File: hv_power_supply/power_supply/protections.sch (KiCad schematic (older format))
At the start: 15 parts, among them J2 CONN_01x02, K2 LI12-1A85(NO), Q2 SSM3K333R, Q3 SSM3K333R, Q4 FQD2N60CTM, U6 CPC1117NTR

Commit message: Update output relay
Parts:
- removed D4: D_Zener_18V, footprints:DO-214AA, symbol formula:D_Zener_18V
- removed D5: Diode_600V_1A_SM, footprints:Diode_600V_1A_SM, symbol formula:Diode_600V_1A_SM
- removed K2: LI12-1A85(NO), footprints:Meder-LI12, symbol formula:LI12-1A85(NO)
- removed Q2: SSM3K333R, footprints:SOT-23F, symbol formula:SSM3K333R
- added F1: F_1A_600V, footprints:Fuse_1A_600V, symbol formula:F_1A_600V
- added K1: CPC1979J, footprints:TO381P2016X515X2916-4, symbol formula:CPC1979J
- added Q4: SSM3K333R, footprints:SOT-23F, symbol formula:SSM3K333R
- renumbered D1 to D4, Q3 to Q2, Q4 to Q3, R1 to R23
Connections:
- wire segments 24 -> 19
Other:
- note added: "Normally Closed SSR"
- note added: "Normally Open SSR"
- note removed: "Normally Closed"
- note removed: "To outside switch"

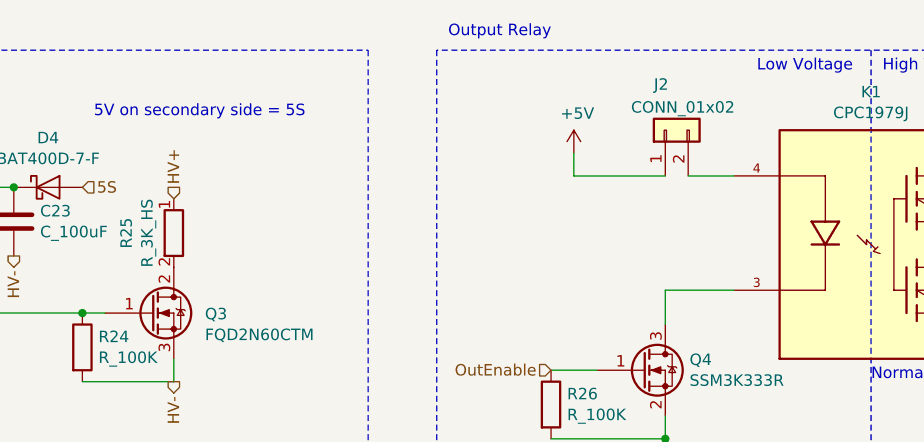
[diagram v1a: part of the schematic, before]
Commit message: Add resistor to output relay
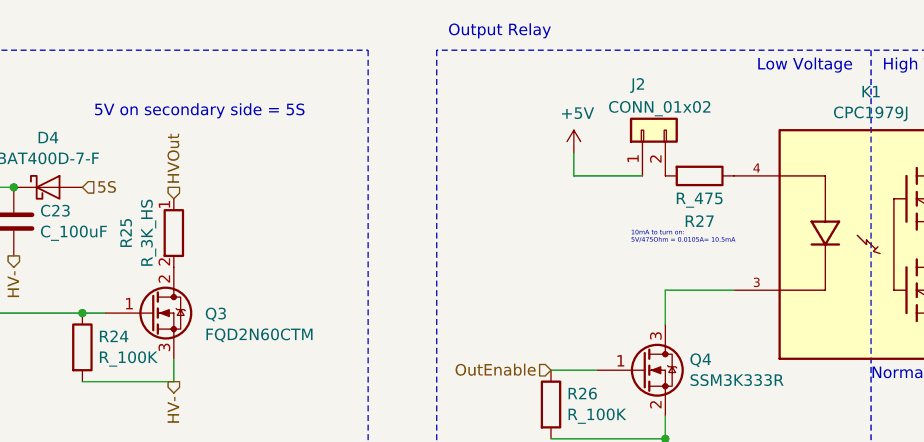
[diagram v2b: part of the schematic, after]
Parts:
- added R27: R_475, footprints:R_0805_OEM, symbol formula:R_475
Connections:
- net HV+: no longer R25.1
- net HVOut: now also R25.1
- net at K1.4: now also R27.1; no longer J2.2 (Pin_2)
- new net: J2.2 (Pin_2), R27.2
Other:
- note added: "10mA to turn on:\n5V/475Ohm = 0.0105A= 10.5mA"
- moved on the sheet: J2
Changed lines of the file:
@@
 $Descr A4 11693 8268
 encoding utf-8
-Sheet 1 1
+Sheet 5 5
 Title ""
 Date ""
@@
 HV-
 Text HLabel 4000 1450 1    50   Input ~ 0
-HV+
+HVOut
 $Comp
 L formula:R_3K_HS R25
@@
 L formula:CONN_01x02 J2
 U 1 1 6035D5F6
-P 6150 1150
-F 0 "J2" V 6350 1200 50  0000 R CNN
-F 1 "CONN_01x02" V 6250 1300 50  0000 R CNN
-F 2 "Connector_PinHeader_2.54mm:PinHeader_1x02_P2.54mm_Vertical" H 6050 1150 50  0001 C CNN
-F 3 "https://katalog.we-online.de/em/datasheet/6130xx11121.pdf" H 6150 1250 50  0001 C CNN
-F 4 "DK" H 6250 1350 50  0001 C CNN "MFN"
-F 5 "732-5315-ND" H 6350 1450 50  0001 C CNN "MPN"
-	1    6150 1150
+P 6050 1150
+F 0 "J2" V 6250 1200 50  0000 R CNN
+F 1 "CONN_01x02" V 6150 1300 50  0000 R CNN
+F 2 "Connector_PinHeader_2.54mm:PinHeader_1x02_P2.54mm_Vertical" H 5950 1150 50  0001 C CNN
+F 3 "https://katalog.we-online.de/em/datasheet/6130xx11121.pdf" H 6050 1250 50  0001 C CNN
+F 4 "DK" H 6150 1350 50  0001 C CNN "MFN"
+F 5 "732-5315-ND" H 6250 1450 50  0001 C CNN "MPN"
+	1    6050 1150
 	0    -1   -1   0
 $EndComp
-Wire Wire Line
-	6450 1350 6250 1350
-Wire Wire Line
-	6150 1350 5750 1350
 Wire Wire Line
 	5750 1350 5750 1250
@@
 Text Notes 7100 900  0    50   ~ 0
 High Voltage
+Text Notes 6000 1650 0    20   ~ 0
+10mA to turn on:\n5V/475Ohm = 0.0105A= 10.5mA
+$Comp
+L formula:R_475 R27
+U 1 1 6039FDDB
+P 6300 1350
+F 0 "R27" V 6500 1350 50  0000 C CNN
+F 1 "R_475" V 6400 1350 50  0000 C CNN
+F 2 "footprints:R_0805_OEM" H 6230 1350 50  0001 C CNN
+F 3 "http://www.yageo.com.tw/exep/pages/download/literatures/PYu-R_INT-thick_7.pdf" H 6380 1350 50  0001 C CNN
+F 4 "DK" H 6300 1350 60  0001 C CNN "MFN"
+F 5 "311-475CRCT-ND" H 6300 1350 60  0001 C CNN "MPN"
+F 6 "https://www.digikey.com/products/en?keywords=311-475CRCT-ND" H 6780 1750 60  0001 C CNN "PurchasingLink"
+	1    6300 1350
+	0    1    1    0
+$EndComp
+Wire Wire Line
+	6050 1350 5750 1350
 $EndSCHEMATC

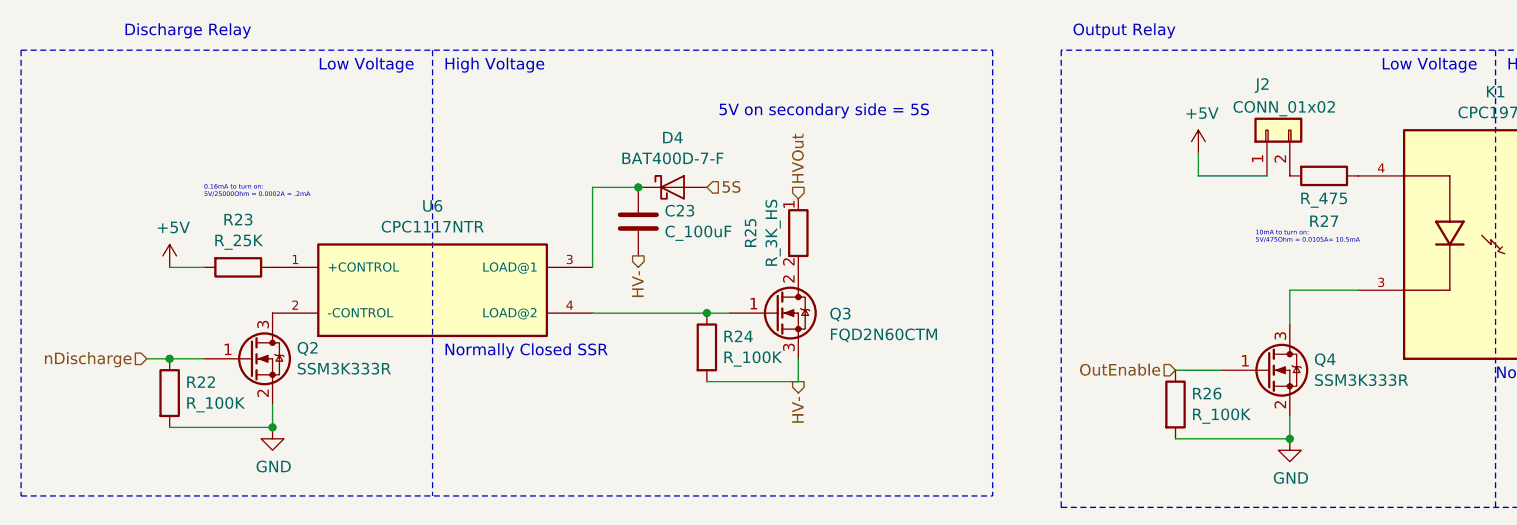
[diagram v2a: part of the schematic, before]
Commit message: Tie inputs to relays together
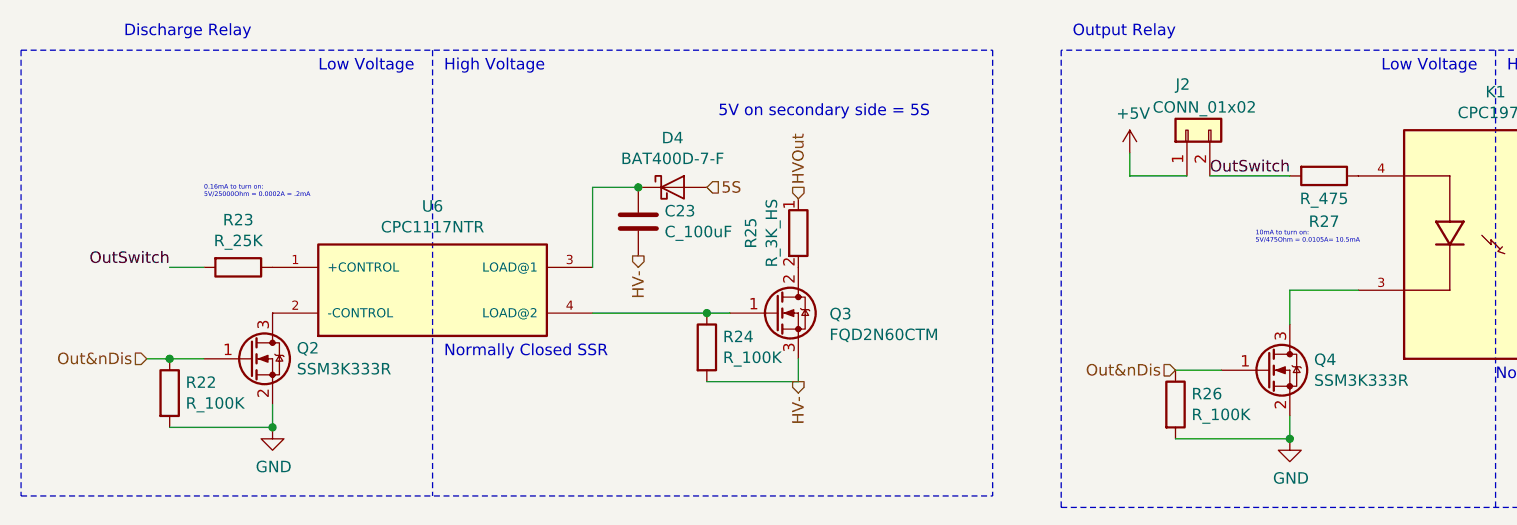
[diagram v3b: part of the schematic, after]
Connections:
- net nDischarge is gone; now on net Out&nDis: Q2.1 (G), R22.1
- net +5V: no longer R23.2
- net OutSwitch: now reaches J2.2 (Pin_2), R27.2
- net OutSwitch: now also R23.2
- net OutEnable renamed Out&nDis
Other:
- moved on the sheet: J2
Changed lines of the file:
@@
 	1250 2450 1700 2450
 Text HLabel 1150 2150 0    50   Input ~ 0
-nDischarge
+Out&nDis
 Wire Wire Line
 	1250 2150 1150 2150
@@
 Connection ~ 3300 1400
 $Comp
-L power:+5V #PWR071
-U 1 1 6029A8EE
-P 1250 1750
-F 0 "#PWR071" H 1250 1600 50  0001 C CNN
-F 1 "+5V" H 1265 1923 50  0000 C CNN
-F 2 "" H 1250 1750 50  0001 C CNN
-F 3 "" H 1250 1750 50  0001 C CNN
-	1    1250 1750
-	1    0    0    -1
-$EndComp
-$Comp
 L formula:R_25K R23
 U 1 1 602A28CD
@@
 L formula:CONN_01x02 J2
 U 1 1 6035D5F6
-P 6050 1150
-F 0 "J2" V 6250 1200 50  0000 R CNN
-F 1 "CONN_01x02" V 6150 1300 50  0000 R CNN
-F 2 "Connector_PinHeader_2.54mm:PinHeader_1x02_P2.54mm_Vertical" H 5950 1150 50  0001 C CNN
-F 3 "https://katalog.we-online.de/em/datasheet/6130xx11121.pdf" H 6050 1250 50  0001 C CNN
-F 4 "DK" H 6150 1350 50  0001 C CNN "MFN"
-F 5 "732-5315-ND" H 6250 1450 50  0001 C CNN "MPN"
-	1    6050 1150
+P 5700 1150
+F 0 "J2" V 5900 1200 50  0000 R CNN
+F 1 "CONN_01x02" V 5800 1300 50  0000 R CNN
+F 2 "Connector_PinHeader_2.54mm:PinHeader_1x02_P2.54mm_Vertical" H 5600 1150 50  0001 C CNN
+F 3 "https://katalog.we-online.de/em/datasheet/6130xx11121.pdf" H 5700 1250 50  0001 C CNN
+F 4 "DK" H 5800 1350 50  0001 C CNN "MFN"
+F 5 "732-5315-ND" H 5900 1450 50  0001 C CNN "MPN"
+	1    5700 1150
 	0    -1   -1   0
 $EndComp
 Wire Wire Line
-	5750 1350 5750 1250
+	5450 1350 5450 1250
 $Comp
 L power:+5V #PWR073
 U 1 1 60366556
-P 5750 1250
-F 0 "#PWR073" H 5750 1100 50  0001 C CNN
-F 1 "+5V" H 5765 1423 50  0000 C CNN
-F 2 "" H 5750 1250 50  0001 C CNN
-F 3 "" H 5750 1250 50  0001 C CNN
-	1    5750 1250
+P 5450 1250
+F 0 "#PWR073" H 5450 1100 50  0001 C CNN
+F 1 "+5V" H 5465 1423 50  0000 C CNN
+F 2 "" H 5450 1250 50  0001 C CNN
+F 3 "" H 5450 1250 50  0001 C CNN
+	1    5450 1250
 	1    0    0    -1
 $EndComp
 Text HLabel 5650 2200 0    50   Input ~ 0
-OutEnable
+Out&nDis
 $Comp
 L formula:R_100K R26
@@
 	0    1    1    0
 $EndComp
-Wire Wire Line
-	6050 1350 5750 1350
+Text Label 5800 1350 0    50   ~ 0
+OutSwitch
+Text Label 1250 1750 2    50   ~ 0
+OutSwitch
+Wire Wire Line
+	5700 1350 5450 1350
+Wire Wire Line
+	5800 1350 6150 1350
 $EndSCHEMATC

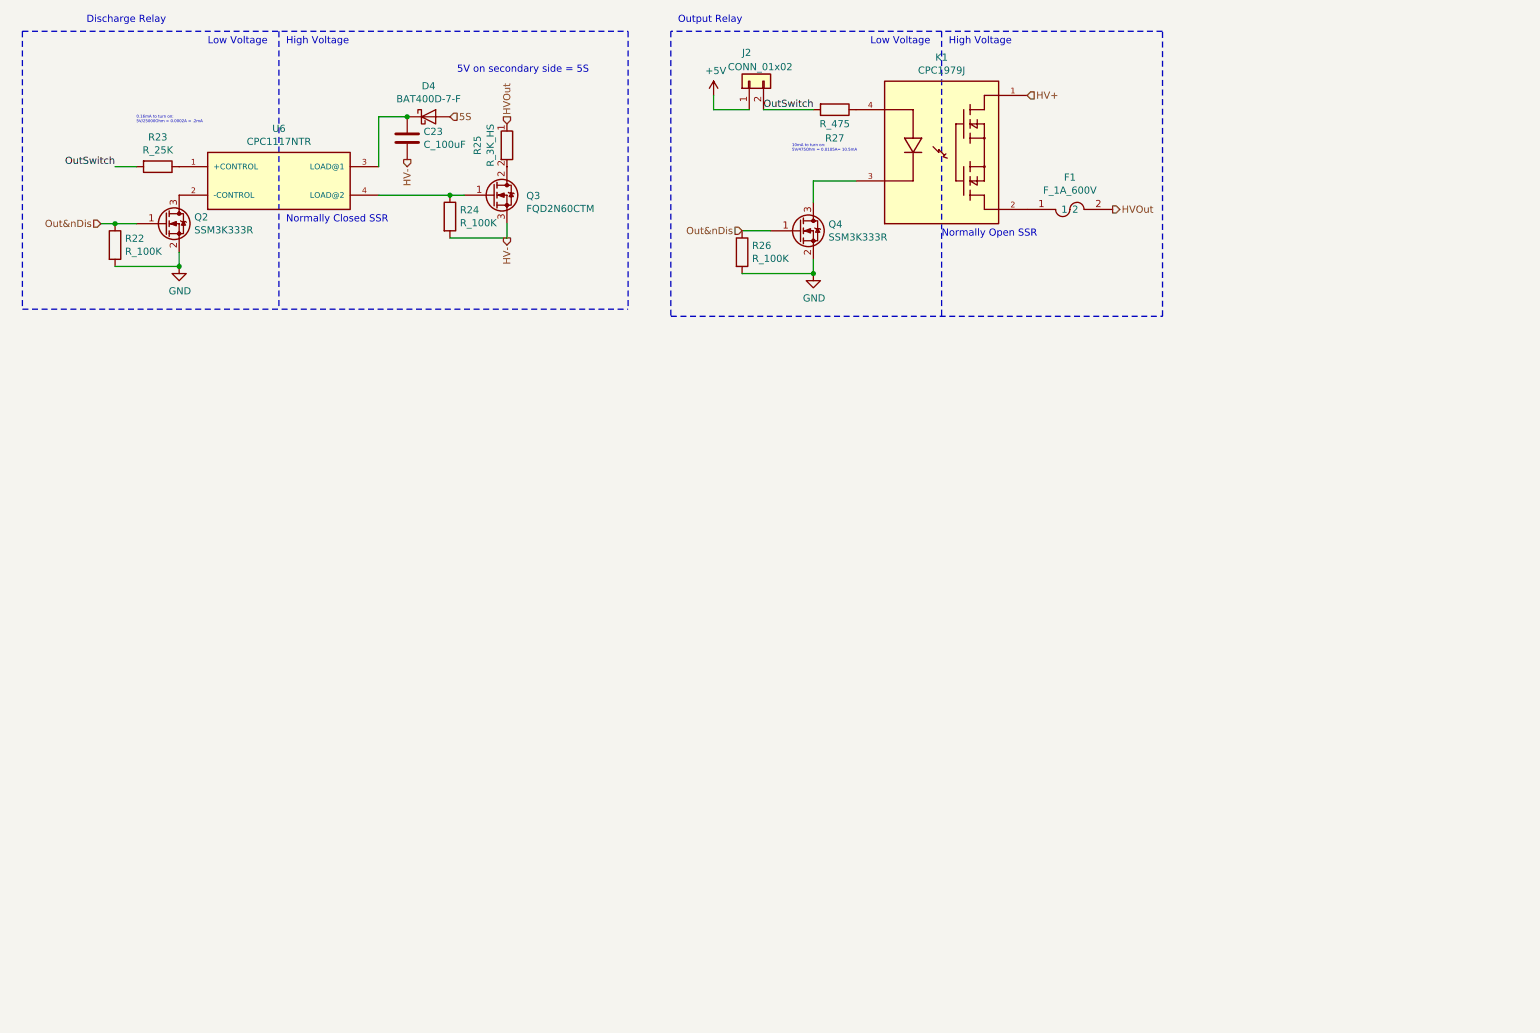
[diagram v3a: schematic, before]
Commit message: make schematic sheets talk to each other
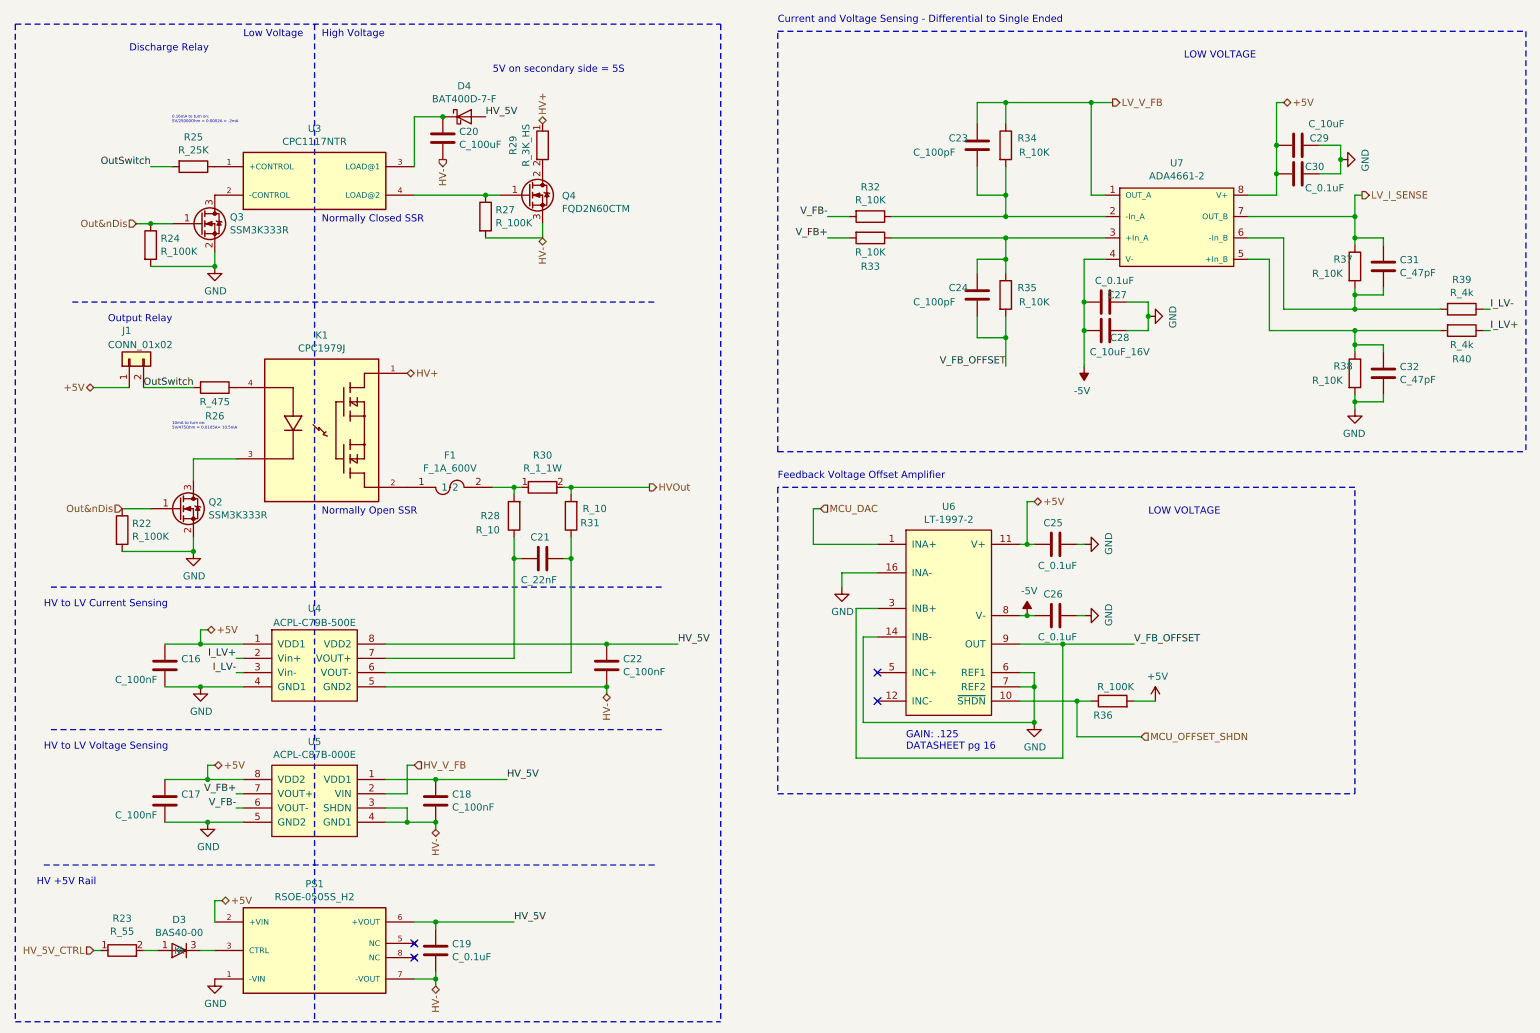
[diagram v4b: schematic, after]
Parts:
- added C16, C17, C18, C22: C_100nF, footprints:C_0603_1608Metric, symbol formula:C_100nF
- added C19, C25, C26, C27, C30: C_0.1uF, footprints:C_0805_OEM, symbol formula:C_0.1uF
- added C21: C_22nF, footprints:C_0805_OEM, symbol formula:C_22nF
- added C23, C24: C_100pF, footprints:C_0805_OEM, symbol formula:C_100pF
- added C28: C_10uF_16V, footprints:C_0805_OEM, symbol formula:C_10uF_16V
- added C29: C_10uF, footprints:C_0805_OEM, symbol formula:C_10uF_16V
- added C31, C32: C_47pF, footprints:C_0805_OEM, symbol formula:C_47pF
- added D3: BAS40-00, Package_TO_SOT_SMD:SOT-23, symbol formula:BAS40-00
- added PS1: RSOE-0505S_H2, footprints:H2, symbol formula:RSOE-0505S_H2
- added R23: R_55, symbol formula:R_55
- added R28, R31: R_10, footprints:R_0805_OEM, symbol formula:R_10
- added R30: R_1_1W, formula:R_2512_LARGE, symbol formula:R_1_1W
- added R32, R33, R34, R35, R37, R38: R_10K, footprints:R_0805_OEM, symbol formula:R_10K
- added R36: R_100K, footprints:R_0805_OEM, symbol formula:R_100K
- added R39, R40: R_4k, footprints:R_0805_OEM, symbol formula:R_4k
- added U4: ACPL-C79B-500E, footprints:SSO-8, symbol formula:ACPL-C79B-500E
- added U5: ACPL-C87B-000E, formula:SSO-8, symbol formula:ACPL-C87B-000E
- added U6: LT-1997-2, formula:16(12)-MSOP, symbol formula:LT-1997-2
- added U7: ADA4661-2, footprints:SOP65P490X110-8N, symbol formula:ADA4661-2
- renumbered C23 to C20, J2 to J1, Q4 to Q2, Q2 to Q3, Q3 to Q4, R26 to R22, R22 to R24, R23 to R25, R27 to R26, R24 to R27, R25 to R29, U6 to U3
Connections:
- net +5V: now also C16.1, C17.1, C25.1, C29.1, C30.2, PS1.2 (+VIN), R36.2, U4.1 (VDD1), U5.8 (VDD2), U6.11 (V+), U7.8 (V+)
- net GND: now also C16.2, C17.2, C25.2, C26.2, C27.2, C28.2, C29.2, C30.1, C32.2, PS1.1 (-VIN), R38.2, U4.4 (GND1), U5.5 (GND2), U6.14 (INB-), U6.16 (INA-), U6.6 (REF1), U6.7 (REF2)
- net HV+: now also R29.1
- net HV-: now also C18.2, C19.2, C22.2, PS1.7 (-VOUT), U4.5 (GND2), U5.3 (SHDN), U5.4 (GND1)
- net HVOut: now also R30.2, R31.2; no longer F1.2, R29.1
- net 5S renamed HV_5V
- net HV_5V: now also C18.1, C19.1, C22.1, PS1.6 (+VOUT), U4.8 (VDD2), U5.1 (VDD1)
- new net: F1.2, R28.2, R30.1
- new net: D3.3 (K), PS1.3 (CTRL)
- new net: C21.1, R28.1, U4.7 (VOUT+)
- new net: C21.2, R31.1, U4.6 (VOUT-)
- new net: C23.2, R32.1, R34.2, U7.2 (-In_A)
- new net: C24.1, R33.1, R35.1, U7.3 (+In_A)
- new net: C32.1, R38.1, R40.2, U7.5 (+In_B)
- new net: C31.2, R37.2, R39.2, U7.6 (-In_B)
- new net: D3.1 (A), R23.2
- new net -5V: C26.1, C27.1, C28.1, U6.8 (V-), U7.4 (V-)
- new net HV_5V_CTRL: R23.1
- new net HV_V_FB: U5.2 (VIN)
- new net I_LV+: R40.1, U4.2 (Vin+)
- new net I_LV-: R39.1, U4.3 (Vin-)
- new net LV_I_SENSE: C31.1, R37.1, U7.7 (OUT_B)
- new net LV_V_FB: C23.1, R34.1, U7.1 (OUT_A)
- new net MCU_DAC: U6.1 (INA+)
- new net MCU_OFFSET_SHDN: R36.1, U6.10 (~SHDN)
- new net V_FB+: R33.2, U5.7 (VOUT+)
- new net V_FB-: R32.2, U5.6 (VOUT-)
- new net V_FB_OFFSET: C24.2, R35.2, U6.3 (INB+), U6.9 (OUT)
- no-connect marks 0 -> 4
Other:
- note added: "Current and Voltage Sensing - Differential to Single Ended"
- note added: "Feedback Voltage Offset Amplifier"
- note added: "GAIN: .125\nDATASHEET pg 16"
- note added: "HV +5V Rail"
- note added: "HV to LV Current Sensing"
- note added: "HV to LV Voltage Sensing"
- note added: "LOW VOLTAGE"
- moved on the sheet: C20, D4, F1, J1, K1, Q2, Q3, Q4, R22, R24, R25, R26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
